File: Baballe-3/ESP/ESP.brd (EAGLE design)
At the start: 46 x 46 mm, 13 parts

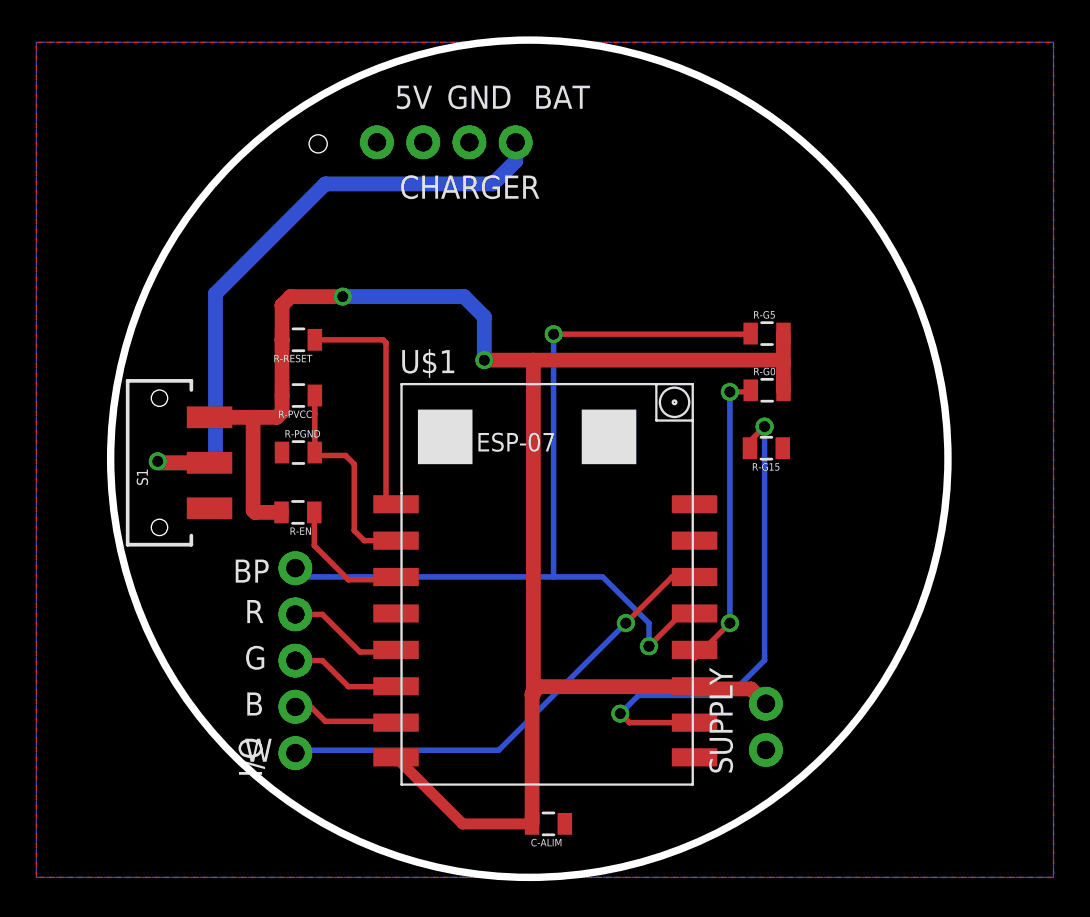
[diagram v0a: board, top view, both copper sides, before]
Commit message: Patch height error
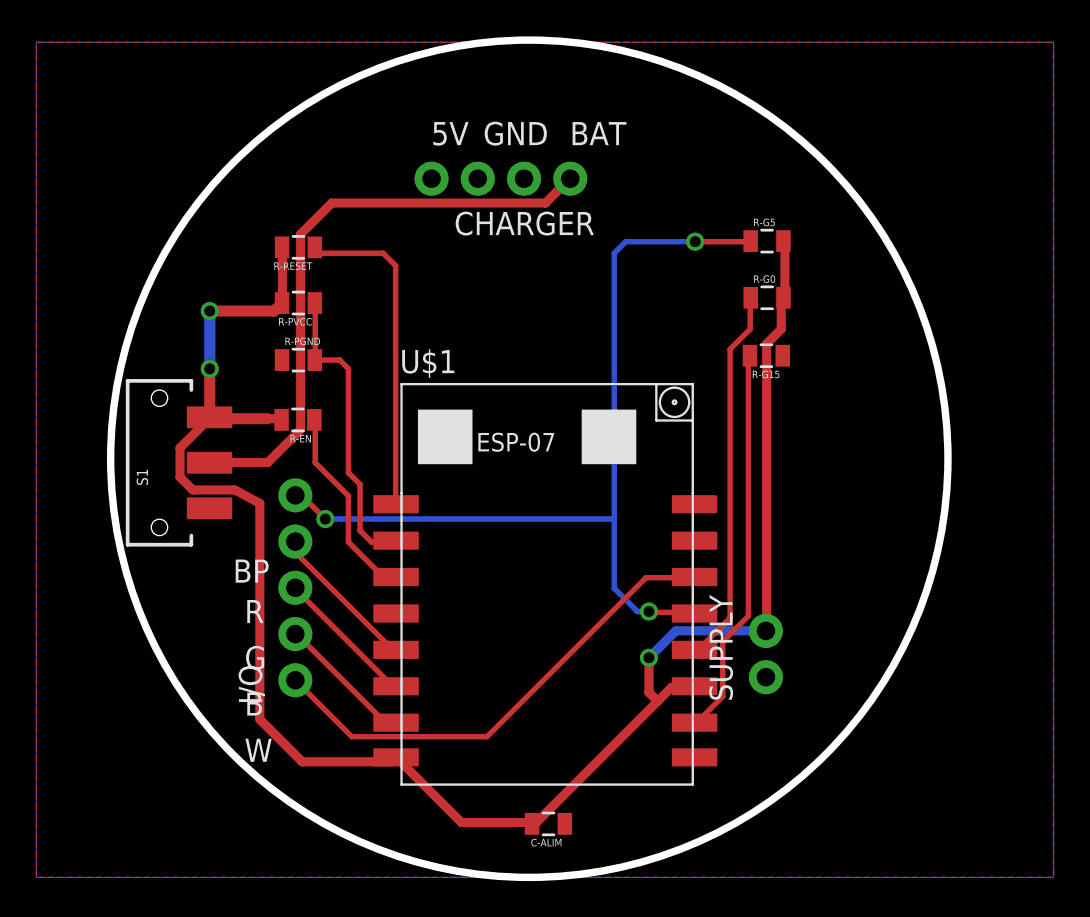
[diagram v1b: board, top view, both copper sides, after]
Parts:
- moved R-G0 5.08 mm to (35.1, 31.8)
- moved R-G15 5.08 mm to (35.0, 28.7)
- moved R-G5 5.08 mm to (35.1, 35.0)
- moved R-PGND 5.08 mm to (9.31, 28.4)
- moved R-EN 5.08 mm to (9.29, 25.1)
- moved R-PVCC 5.08 mm to (9.32, 31.6)
- moved R-RESET 5.08 mm to (9.32, 34.6)
- moved SUPPLY 4.00 mm to (35.0, 11.0)
- moved I/O 4.00 mm to (9.15, 10.8)
- moved CHARGER 3.61 mm to (24.3, 38.4)
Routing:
- net N$1: track 27.7 -> 21.6 mm, vias 2 -> 0
- net I_VBAT: track 11.7 -> 16.9 mm
- net N$9: track 13.4 -> 18.0 mm
- net N$10: track 7.15 -> 11.2 mm
- net VCC: track 98.6 -> 102.6 mm, vias 2 -> 3
- net N$6: track 17.3 -> 20.7 mm, vias 2 -> 0
- net V_BATT: track 35.8 -> 32.6 mm, vias 1 -> 0
- net O_BLUE: track 6.44 -> 8.36 mm
- net O_RED: track 6.14 -> 7.82 mm
- net O_GREEN: track 5.89 -> 7.55 mm
- net O_WHITE: track 25.9 -> 26.8 mm, vias 1 -> 0
- net GND: track 0.00 -> 0.91 mm
- net I_BUTTON: track 49.5 -> 49.9 mm, vias 2 -> 3
